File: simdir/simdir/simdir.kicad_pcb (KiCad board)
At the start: 4 copper layers, 249.9 x 160.1 mm, 318 parts, among them J1 Conn_Coaxial, J2 Conn_Coaxial, J3 Conn_Coaxial, J4 Conn_02x05_Odd_Even, J5 Conn_Coaxial, J6 Conn_01x02, Q1 BC847, Q10 BC847, Q11 BC847, Q12 BC847, Q13 BC847, Q14 BC847, Q15 BC847, Q16 BC847, Q17 BC847, Q18 BC847, Q19 BC847, Q2 BC847, Q20 BC847, Q21 BC847, Q22 BC847, Q23 BC847, Q24 BC847, Q25 BC847, Q26 BC847, Q27 BC847, Q28 BC847, Q29 BC847, Q3 BC847, Q30 BC847, Q31 BC847, Q32 BC847, Q33 BC847, Q34 BC847, Q35 BC847, Q36 BC847, Q37 BC847, Q38 BC847, Q39 BC847, Q4 BC847, Q40 BC847, Q41 BC847, Q42 BC847, Q43 BC847, Q44 BC847, Q45 BC847, Q46 BC847, Q47 BC847, Q48 BC847, Q5 BC847, Q6 BC847, Q7 BC847, Q8 BC847, Q9 BC847, U100 AS179-92LF, U101 AS179-92LF, U102 AS179-92LF, U103 AS179-92LF, U104 AS179-92LF, U105 AS179-92LF, U106 AS179-92LF, U17 LTV-847S, U18 LTV-847S, U19 74HCT595, U20 74HCT595, U25 LTV-847S, U30 LTV-847S, U39 74HCT595, U44 LTV-847S, U49 LTV-847S, U58 LM2940CT-5.0, U59 AS179-92LF, U60 AS179-92LF, U61 AS179-92LF, U62 AS179-92LF, U63 AS179-92LF, U64 AS179-92LF, U65 AS179-92LF, U66 AS179-92LF, U67 AS179-92LF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

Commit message: Fixed E block.
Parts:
- C37, C38, C40, C41, C43, C44, C46, C47, C49, C50, C52, C53, C55, C56, C58, C59, C61, C62: moved to B.Cu
- moved C62 167.8 mm to (181.2, 88.0), turned to 90 degrees
- moved C59 165.6 mm to (163.7, 88.2), turned to 90 degrees
- moved C61 164.4 mm to (181.1, 138.4), turned to 90 degrees
- moved C34 164.3 mm to (178.4, 106.6)
- moved C35 162.0 mm to (177.8, 56.0)
- moved C58 150.3 mm to (163.6, 138.6), turned to 90 degrees
- moved C56 149.4 mm to (146.7, 88.2), turned to 90 degrees
- moved C31 148.7 mm to (162.6, 106.6)
- moved C32 145.9 mm to (161.9, 56.0)
- moved U105 136.4 mm to (173.7, 106.6)
- moved C53 134.5 mm to (131.4, 88.2), turned to 90 degrees
- moved C55 133.2 mm to (146.6, 138.6), turned to 90 degrees
- moved C28 131.5 mm to (145.1, 106.6)
- moved U102 130.5 mm to (168.1, 106.6), turned to 180 degrees
- moved C29 128.2 mm to (144.4, 56.0)
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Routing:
- net RF_GND: track 696.1 -> 616.5 mm, vias 752 -> 782
- net (no net): track 75.6 -> 0.00 mm
- net Net-(U61-V2): track 291.6 -> 331.6 mm
- net Net-(U100-V1): track 103.2 -> 75.8 mm
- net Net-(U103-V2): track 76.7 -> 102.1 mm, vias 4 -> 2
- net Net-(Q41-C): track 49.3 -> 73.5 mm
- net Net-(U64-V1): track 267.3 -> 245.9 mm, vias 3 -> 5
- net Net-(U60-V2): track 291.6 -> 311.6 mm, vias 2 -> 3
- net Net-(U85-V2): track 142.9 -> 158.9 mm, vias 3 -> 2
- net Net-(U73-V2): track 164.2 -> 179.2 mm
- net Net-(U91-V2): track 113.7 -> 127.0 mm
- net Net-(U84-V2): track 144.3 -> 131.2 mm, vias 3 -> 4
- net Net-(U63-V1): track 267.3 -> 280.2 mm, vias 3 -> 4
- net Net-(U72-V2): track 164.2 -> 175.2 mm
- net Net-(U102-V2): track 76.7 -> 66.7 mm
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
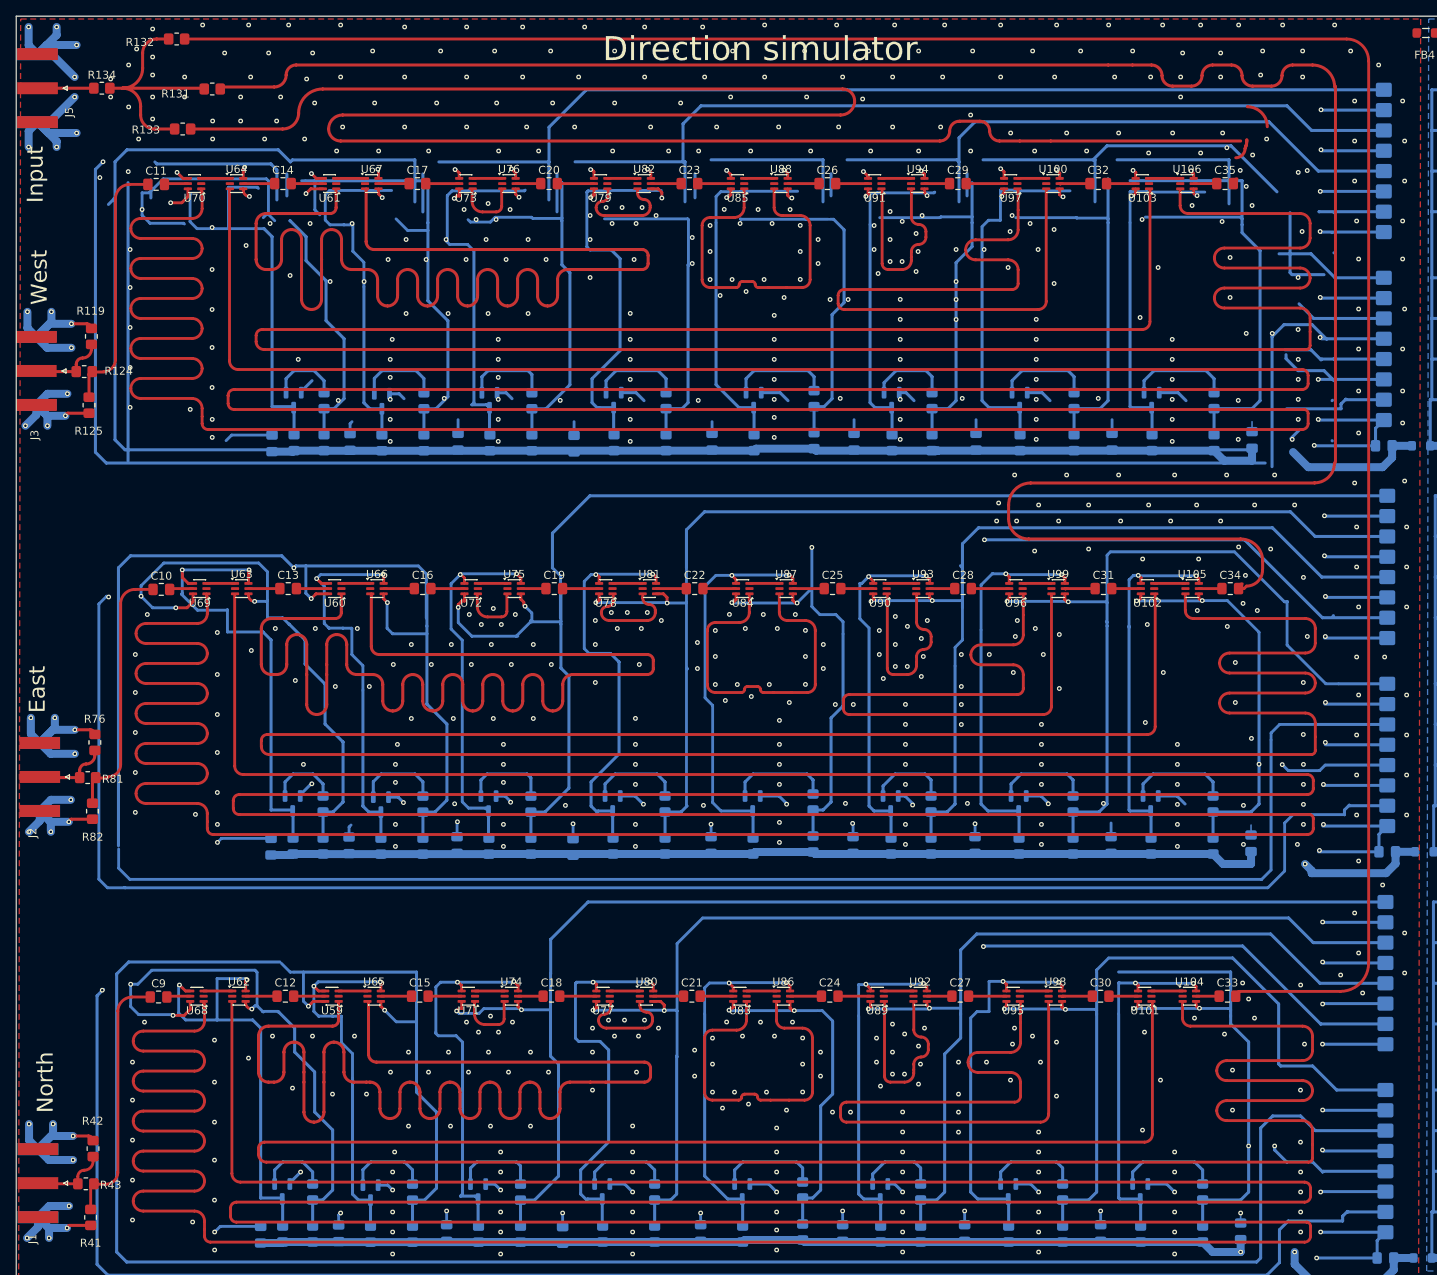
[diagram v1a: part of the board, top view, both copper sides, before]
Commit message: Fixed routing & delay paths.
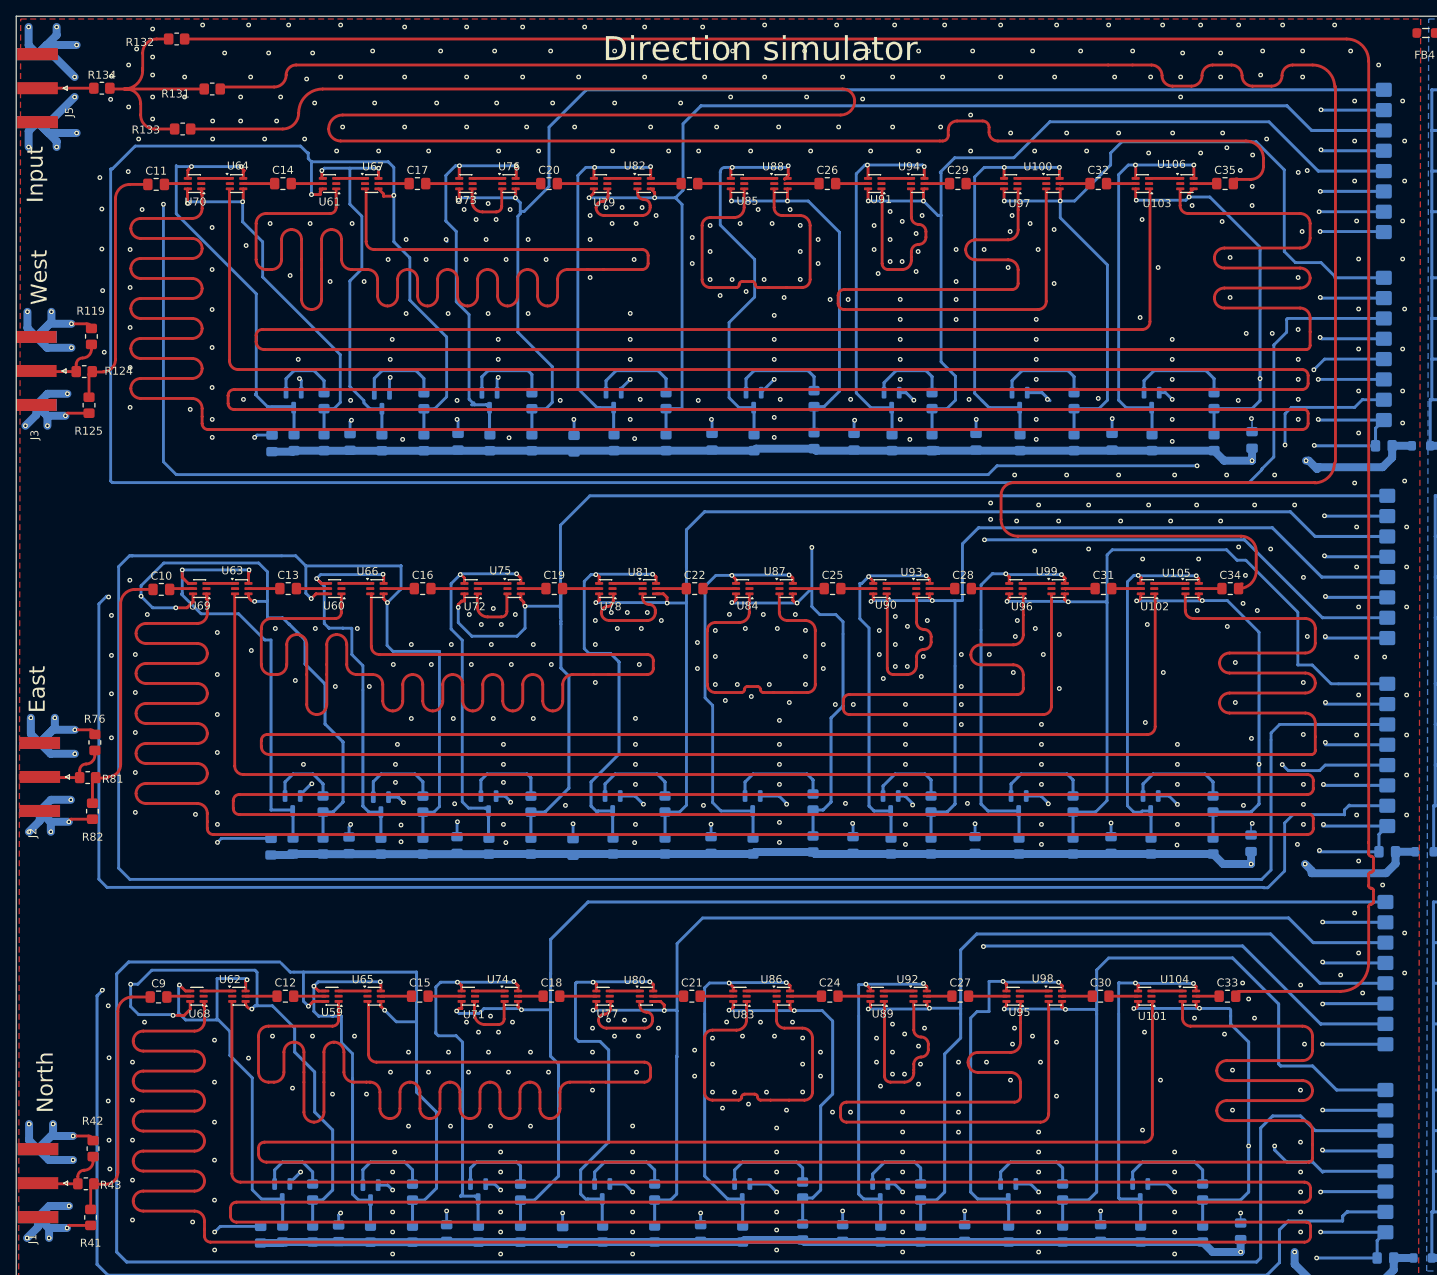
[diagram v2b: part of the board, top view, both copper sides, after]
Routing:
- net RF_GND: track 616.5 -> 496.4 mm, vias 782 -> 804
- net Net-(U103-V2): track 102.1 -> 66.0 mm, vias 2 -> 4
- net Net-(U61-V2): track 331.6 -> 301.0 mm
- net Net-(U100-V1): track 75.8 -> 102.8 mm
- net Net-(U85-V2): track 158.9 -> 132.3 mm, vias 2 -> 3
- net Net-(Q41-C): track 73.5 -> 53.1 mm
- net Net-(U101-V2): track 85.1 -> 66.3 mm
- net Net-(U91-V2): track 127.0 -> 109.5 mm
- net Net-(U73-V2): track 179.2 -> 162.3 mm
- net Net-(U79-V2): track 156.9 -> 144.9 mm
- net Net-(U60-V2): track 311.6 -> 302.2 mm, vias 3 -> 2
- net Net-(Q44-C): track 54.4 -> 48.1 mm
- net Net-(U64-V1): track 245.9 -> 240.9 mm
- net Net-(Q48-C): track 44.7 -> 49.4 mm
- net /channel3/RF-In: track 279.0 -> 282.9 mm
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
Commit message: Fixed PCB layout.
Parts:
- removed FB4: FerriteBead, Inductor_SMD:L_0805_2012Metric_Pad1.05x1.20mm_HandSolder
- added H1: MountingHole_Pad, MountingHole:MountingHole_4.3mm_M4_Pad_Via, F.Cu at (271.0, 40.8)
- added H2: MountingHole_Pad, MountingHole:MountingHole_4.3mm_M4_Pad_Via, F.Cu at (270.2, 187.9)
- added H3: MountingHole_Pad, MountingHole:MountingHole_4.3mm_M4_Pad_Via, F.Cu at (33.9, 150.4)
- added H4: MountingHole_Pad, MountingHole:MountingHole_4.3mm_M4_Pad_Via, F.Cu at (33.9, 99.0)
- added NT1: NetTie_2, NetTie:NetTie-2_THT_Pad1.0mm, F.Cu at (204.4, 37.1)
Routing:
- net Net-(Q42-C): track 46.6 -> 47.2 mm
- net RF_GND: vias 804 -> 828
